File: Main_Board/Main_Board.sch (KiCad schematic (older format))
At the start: 40 parts, among them J3 BATT_IN, Q1 Q_PMOS_GDS, U1 TEENSY_4_1_MASTER, U2 TEENSY_4_1_SLAVE

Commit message: Started Light PCB
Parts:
- added R?: 100k, symbol Device:R_Small
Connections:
- wire segments 215 -> 223
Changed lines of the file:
@@
 	11600 2400 11600 2300
 Wire Wire Line
-	11600 3200 11600 3100
+	11600 3200 11600 3150
 $Comp
 L Switch:SW_SPST SW?
@@
 Text GLabel 2500 6850 0    50   Input ~ 0
 P4
-Text GLabel 2000 5250 0    50   Input ~ 0
+Text GLabel 2500 6450 0    50   Input ~ 0
 ~WR
-Text GLabel 1850 5350 0    50   Input ~ 0
+Text GLabel 4700 6650 2    50   Input ~ 0
 ~CS
-Text GLabel 1850 5150 0    50   Input ~ 0
+Text GLabel 2350 6350 0    50   Input ~ 0
 ~EN
 Text GLabel 4300 8050 2    50   Input ~ 0
 D
-Text GLabel 2000 4950 0    50   Input ~ 0
+Text GLabel 4300 6550 2    50   Input ~ 0
 LIGHT_EN
 Text GLabel 5350 6750 0    50   Output ~ 0
@@
 	1    0    0    -1
 $EndComp
+Wire Wire Line
+	4300 6550 4200 6550
+Wire Wire Line
+	2500 6450 2600 6450
+Wire Wire Line
+	2350 6350 2600 6350
+Wire Wire Line
+	4700 6650 4200 6650
+$Comp
+L power:+VDC #PWR?
+U 1 1 6200D369
+P 11250 3100
+F 0 "#PWR?" H 11250 3000 50  0001 C CNN
+F 1 "+VDC" H 11250 3375 50  0000 C CNN
+F 2 "" H 11250 3100 50  0001 C CNN
+F 3 "" H 11250 3100 50  0001 C CNN
+	1    11250 3100
+	1    0    0    -1
+$EndComp
+$Comp
+L Device:R_Small R?
+U 1 1 6200E122
+P 11400 3150
+F 0 "R?" H 11459 3196 50  0000 L CNN
+F 1 "100k" H 11459 3105 50  0000 L CNN
+F 2 "" H 11400 3150 50  0001 C CNN
+F 3 "~" H 11400 3150 50  0001 C CNN
+	1    11400 3150
+	0    1    1    0
+$EndComp
+Wire Wire Line
+	11500 3150 11600 3150
+Connection ~ 11600 3150
+Wire Wire Line
+	11600 3150 11600 3100
+Wire Wire Line
+	11250 3100 11250 3150
+Wire Wire Line
+	11250 3150 11300 3150
 $EndSCHEMATC

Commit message: Finalizing Main PCB Sch
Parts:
- added J?: HR-SR04_R_CONN, symbol Connector_Generic:Conn_01x04
- added J?: HR-SR04_L_CONN, symbol Connector_Generic:Conn_01x04
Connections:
- net labels added: ECHO_L, ECHO_R, TRIG_L, TRIG_R
- wire segments 223 -> 239
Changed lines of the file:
@@
 	1    0    0    -1
 $EndComp
+Text GLabel 12950 8550 0    50   Output ~ 0
+P0
 Text GLabel 12950 8450 0    50   Output ~ 0
-P0
-Text GLabel 12950 8550 0    50   Output ~ 0
 P1
+Text GLabel 12950 8750 0    50   Output ~ 0
+P2
 Text GLabel 12950 8650 0    50   Output ~ 0
-P2
-Text GLabel 12950 8750 0    50   Output ~ 0
 P3
 Text GLabel 12950 8850 0    50   Output ~ 0
@@
 Text GLabel 4300 8050 2    50   Input ~ 0
 D
-Text GLabel 4300 6550 2    50   Input ~ 0
-LIGHT_EN
 Text GLabel 5350 6750 0    50   Output ~ 0
 HOLD_SW
@@
 Wire Wire Line
 	8500 7500 8550 7500
-Text GLabel 8450 6300 0    50   Input ~ 0
+Text GLabel 8450 6300 0    50   Output ~ 0
 MAGN_SDA
-Text GLabel 8450 6400 0    50   Input ~ 0
+Text GLabel 8450 6400 0    50   Output ~ 0
 MAGN_SCL
 Wire Wire Line
@@
 Wire Wire Line
 	8450 6400 8550 6400
-$Comp
-L power:+5V #PWR?
-U 1 1 62126097
-P 8500 6150
-F 0 "#PWR?" H 8500 6000 50  0001 C CNN
-F 1 "+5V" H 8515 6323 50  0000 C CNN
-F 2 "" H 8500 6150 50  0001 C CNN
-F 3 "" H 8500 6150 50  0001 C CNN
-	1    8500 6150
-	1    0    0    -1
-$EndComp
 Wire Wire Line
 	8500 6150 8500 6200
@@
 Wire Wire Line
 	8500 6500 8550 6500
-Text GLabel 7200 8150 2    50   Input ~ 0
+Text GLabel 7200 8150 2    50   Output ~ 0
 OLED_SDA
-Text GLabel 7200 8250 2    50   Input ~ 0
+Text GLabel 7200 8250 2    50   Output ~ 0
 OLED_SCL
 Text GLabel 7200 8050 2    50   Input ~ 0
@@
 Wire Wire Line
 	11250 3150 11300 3150
+$Comp
+L Connector_Generic:Conn_01x04 J?
+U 1 1 62000862
+P 9950 6300
+F 0 "J?" H 10030 6292 50  0000 L CNN
+F 1 "HR-SR04_R_CONN" H 10030 6201 50  0000 L CNN
+F 2 "" H 9950 6300 50  0001 C CNN
+F 3 "~" H 9950 6300 50  0001 C CNN
+	1    9950 6300
+	1    0    0    -1
+$EndComp
+$Comp
+L Connector_Generic:Conn_01x04 J?
+U 1 1 62000F7B
+P 9950 7350
+F 0 "J?" H 10030 7342 50  0000 L CNN
+F 1 "HR-SR04_L_CONN" H 10030 7251 50  0000 L CNN
+F 2 "" H 9950 7350 50  0001 C CNN
+F 3 "~" H 9950 7350 50  0001 C CNN
+	1    9950 7350
+	1    0    0    -1
+$EndComp
+$Comp
+L power:+3.3V #PWR?
+U 1 1 62001B8E
+P 8500 6150
+F 0 "#PWR?" H 8500 6000 50  0001 C CNN
+F 1 "+3.3V" H 8515 6323 50  0000 C CNN
+F 2 "" H 8500 6150 50  0001 C CNN
+F 3 "" H 8500 6150 50  0001 C CNN
+	1    8500 6150
+	1    0    0    -1
+$EndComp
+$Comp
+L power:GND #PWR?
+U 1 1 62002A38
+P 9700 6550
+F 0 "#PWR?" H 9700 6300 50  0001 C CNN
+F 1 "GND" H 9705 6377 50  0000 C CNN
+F 2 "" H 9700 6550 50  0001 C CNN
+F 3 "" H 9700 6550 50  0001 C CNN
+	1    9700 6550
+	1    0    0    -1
+$EndComp
+$Comp
+L power:+5V #PWR?
+U 1 1 62002DEB
+P 9700 7200
+F 0 "#PWR?" H 9700 7050 50  0001 C CNN
+F 1 "+5V" H 9715 7373 50  0000 C CNN
+F 2 "" H 9700 7200 50  0001 C CNN
+F 3 "" H 9700 7200 50  0001 C CNN
+	1    9700 7200
+	1    0    0    -1
+$EndComp
+$Comp
+L power:GND #PWR?
+U 1 1 6200332C
+P 9700 7600
+F 0 "#PWR?" H 9700 7350 50  0001 C CNN
+F 1 "GND" H 9705 7427 50  0000 C CNN
+F 2 "" H 9700 7600 50  0001 C CNN
+F 3 "" H 9700 7600 50  0001 C CNN
+	1    9700 7600
+	1    0    0    -1
+$EndComp
+$Comp
+L power:+5V #PWR?
+U 1 1 62003657
+P 9700 6150
+F 0 "#PWR?" H 9700 6000 50  0001 C CNN
+F 1 "+5V" H 9715 6323 50  0000 C CNN
+F 2 "" H 9700 6150 50  0001 C CNN
+F 3 "" H 9700 6150 50  0001 C CNN
+	1    9700 6150
+	1    0    0    -1
+$EndComp
+Wire Wire Line
+	9700 6150 9700 6200
+Wire Wire Line
+	9700 6200 9750 6200
+Wire Wire Line
+	9700 6550 9700 6500
+Wire Wire Line
+	9700 6500 9750 6500
+Wire Wire Line
+	9700 7200 9700 7250
+Wire Wire Line
+	9700 7250 9750 7250
+Wire Wire Line
+	9700 7600 9700 7550
+Wire Wire Line
+	9700 7550 9750 7550
+Text GLabel 9650 7350 0    50   Output ~ 0
+TRIG_L
+Text GLabel 9650 6300 0    50   Output ~ 0
+TRIG_R
+Text GLabel 9650 6400 0    50   Output ~ 0
+ECHO_R
+Text GLabel 9650 7450 0    50   Output ~ 0
+ECHO_L
+Wire Wire Line
+	9650 6300 9750 6300
+Wire Wire Line
+	9650 6400 9750 6400
+Wire Wire Line
+	9650 7350 9750 7350
+Wire Wire Line
+	9650 7450 9750 7450
+Text GLabel 2500 7350 0    50   Input ~ 0
+ECHO_R
+Text GLabel 2500 7250 0    50   Input ~ 0
+TRIG_R
+Wire Wire Line
+	2500 7250 2600 7250
+Wire Wire Line
+	2500 7350 2600 7350
+Text GLabel 2500 6650 0    50   Input ~ 0
+ECHO_L
+Text GLabel 4300 6550 2    50   Input ~ 0
+LIGHT_EN
+Text GLabel 2500 6550 0    50   Input ~ 0
+TRIG_L
+Wire Wire Line
+	2500 6550 2600 6550
+Wire Wire Line
+	2500 6650 2600 6650
 $EndSCHEMATC

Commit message: Finalized Pin layout, started redesigned Buck
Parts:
- removed C?: 0.1u, symbol Device:C
- removed C?: 47u, symbol Device:C
- removed C?: 10n, symbol Device:C_Small
- removed C?: 6.8n, symbol Device:C_Small
- removed C?: 22u, symbol Device:C
- removed L?: 8.2u, symbol Device:L
- removed R?: 100k, symbol Device:R
- removed R?: 45.3k, symbol Device:R_Small
- removed R?: 10k, symbol Device:R_Small
- removed R?: 6.8k, symbol Device:R_Small
- removed U?: AP6503, symbol Regulator_Switching:AP6503
- added C? (x8): C_Small, symbol Device:C_Small
- added D? (x2): WS2812B, LED_SMD:LED_WS2812B_PLCC4_5.0x5.0mm_P3.2mm, symbol LED:WS2812B
- added L?: L_Small, symbol Device:L_Small
- added R? (x5): R_Small, symbol Device:R_Small
- added U?: SiC467ED, symbol Main_Board:SiC467ED
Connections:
- wire segments 239 -> 284
- no-connect marks 19 -> 20
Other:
- moved on the sheet: D1, D?, J3, J?, Q1, Q?, R1, R?, SW?, U?

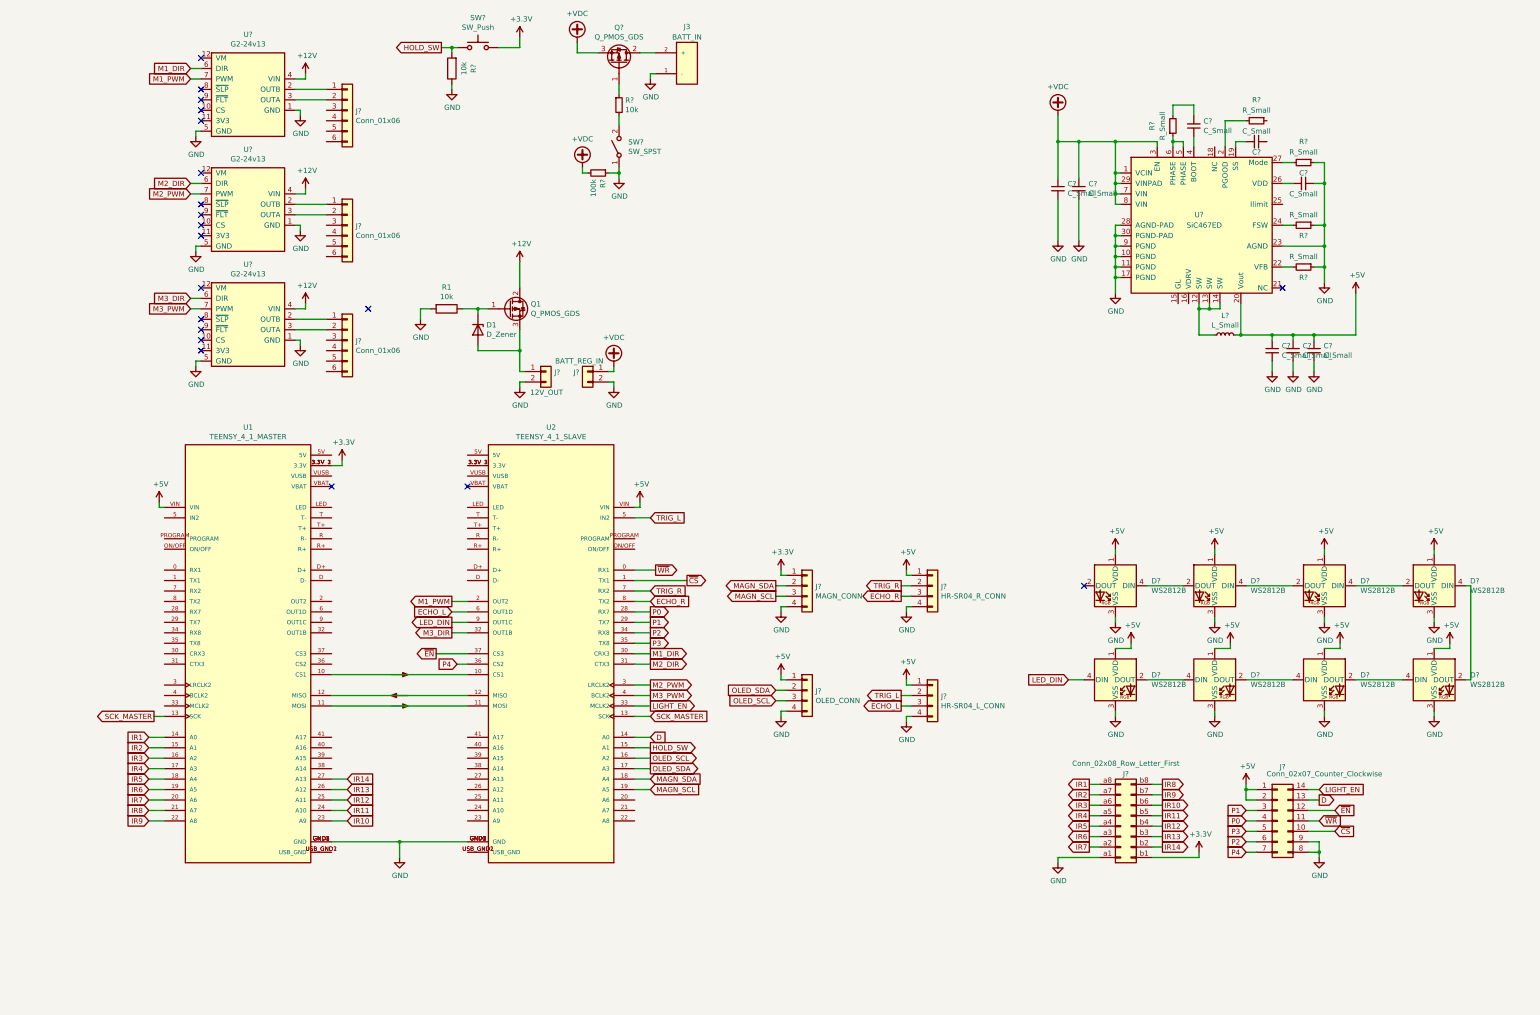
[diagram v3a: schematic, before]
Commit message: added light gate
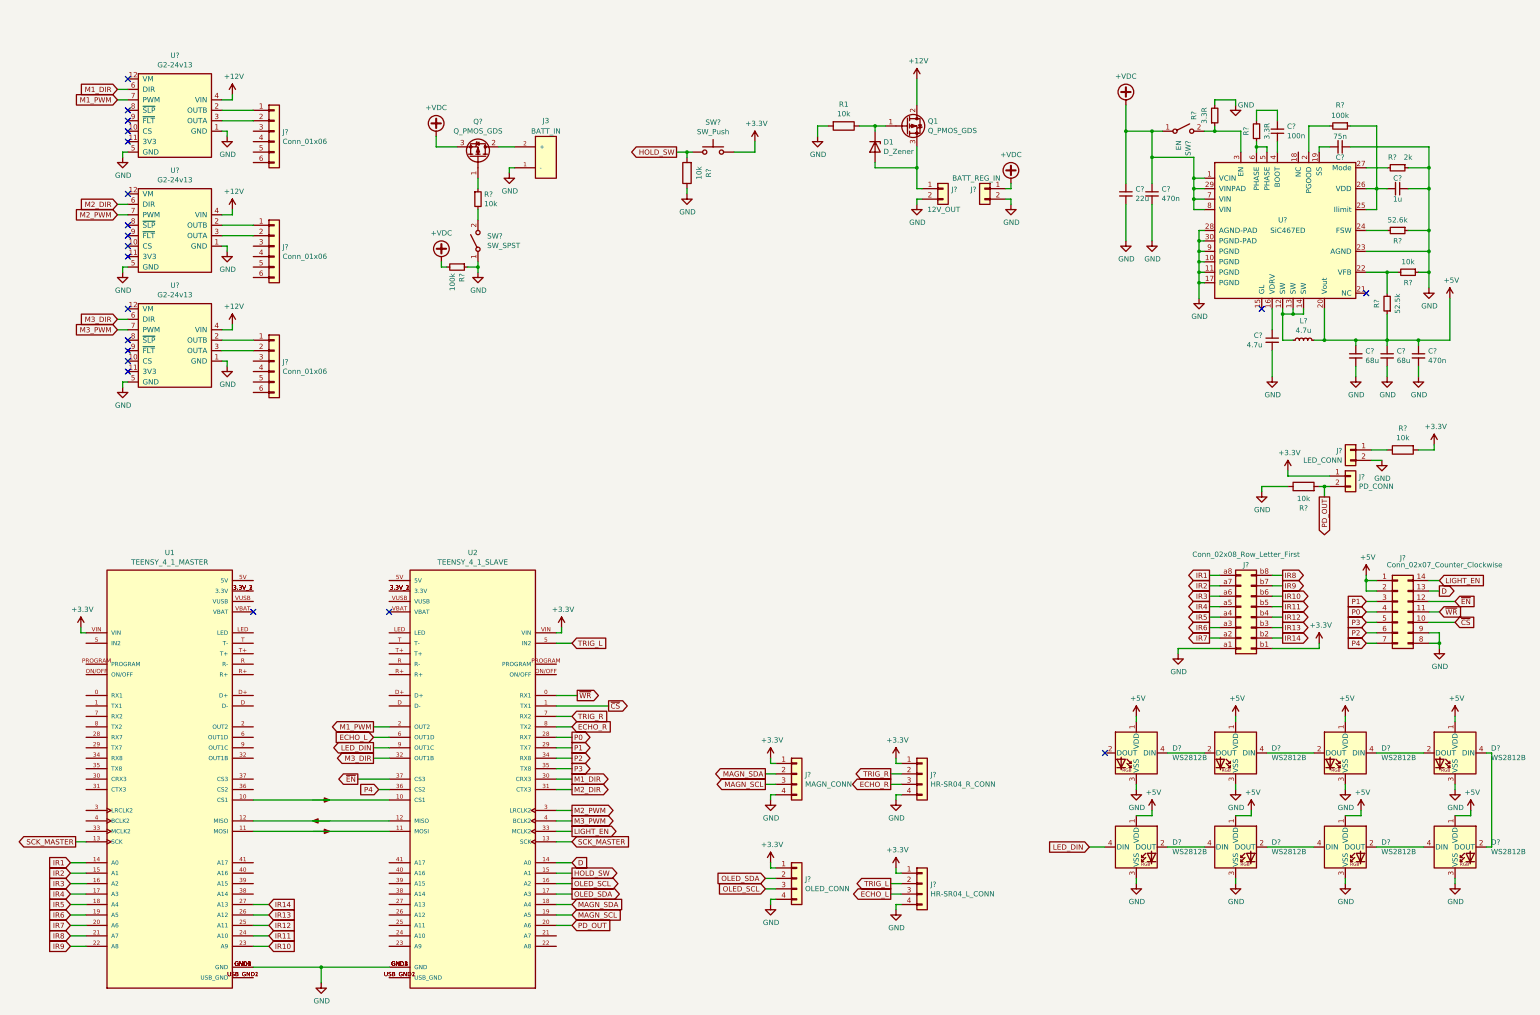
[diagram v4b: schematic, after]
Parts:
- added C?: 4.7u, symbol Device:C_Small
- added J?: PD_CONN, symbol Connector_Generic:Conn_01x02
- added J?: LED_CONN, symbol Connector_Generic:Conn_01x02
- added R?: 52.5k, symbol Device:R_Small
- added R?: 3.3R, symbol Device:R_Small
- added R? (x2): 10k, symbol Device:R
- added SW?: EN, symbol Switch:SW_SPST
- C?: value C_Small -> 22u
- C? (x2): value C_Small -> 470n
- C? (x2): value C_Small -> 68u
- C?: value C_Small -> 1u
- C?: value C_Small -> 75n
- C?: value C_Small -> 100n
- L?: value L_Small -> 4.7u
- R?: value R_Small -> 52.6k
- R?: value R_Small -> 2k
- R?: value R_Small -> 10k
- R?: value R_Small -> 3.3R
- R?: value R_Small -> 100k
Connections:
- net +3V3: now also J?.1 (Pin_1), J?.1 (Pin_1), J?.1 (Pin_1), U1.VIN, U2.VIN, J?.1 (Pin_1), R?.2; no longer U1.3.3V_1 (3.3V), U1.3.3V_2 (3.3V), U1.3.3V_3 (3.3V)
- net +5V: now also R?.1; no longer J?.1 (Pin_1), J?.1 (Pin_1), J?.1 (Pin_1), U1.VIN, U2.VIN
- net +VDC: now also SW?.1 (A); no longer U?.3 (EN)
- net GND: now also C?.1, C?.2, J?.2 (Pin_2), R?.1, R?.2
- net PD_OUT: now reaches U2.20 (A6)
- net PD_OUT: now also J?.2 (Pin_2), R?.2
- net at U?.16 (VDRV): now also C?.1
- net at R?.2, U?.22 (VFB): now also R?.2
- net at U?.25 (Ilimit): now also C?.2, R?.1, U?.26 (VDD)
- new net: U1.3.3V_1 (3.3V), U1.3.3V_2 (3.3V), U1.3.3V_3 (3.3V)
- new net: R?.1, SW?.2 (B), U?.3 (EN)
- new net: J?.1 (Pin_1), R?.1
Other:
- moved on the sheet: C?, D1, D?, J3, J?, L?, Q1, Q?, R1, R?, SW?, U1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

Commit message: Finished Main PCB schematic
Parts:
- C?: value 22u -> 10u
- C? (x2): value 68u -> 22u
- C?: value 470n -> 220n
- L?: value 4.7u -> 2.2u
- R?: value 52.5k -> 17k5
- R?: value 3.3R -> 100k
- R?: value 52.6k -> 34k7
- R?: value 10k -> 5k6
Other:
- note added: "12V Buck-Boost"
- note added: "3.3V Buck"
- note added: "Battery Input"
- note added: "Compass"
- note added: "Connectors"
- note added: "Hold Switch"
- note added: "Indicator LEDs"
- note added: "Light Gate Connectors"
- note added: "Microcontrollers"
- note added: "Motor Drivers"
- note added: "OLED"
- note added: "PCB Connectors"
- note added: "Sonar Left"
- note added: "Sonar Right"
- moved on the sheet: D?, J?, U1, U2

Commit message: Some small alterations to the main pcb sch
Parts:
- removed D1: D_Zener, symbol Device:D_Zener
- removed R1: 10k, symbol Device:R
- added D1, D10, D11: LED, LED_SMD:LED_0805_2012Metric, symbol Device:LED
- added D12: 20V, symbol Device:D_Zener_Small
- added R1, R15, R16, R17: 10k, symbol Device:R_Small
- added R14, R18: 100k, symbol Device:R_Small
- added SW4: SW_SPST, symbol Switch:SW_SPST
- C1, C6, C7: renamed from C?; footprint (none) -> Capacitor_SMD:C_1210_3225Metric
- C2, C3, C4, C5, C8, C9: renamed from C?; footprint (none) -> Capacitor_SMD:C_0603_1608Metric
- J1, J2, J3: renamed from J?; footprint (none) -> Connector_JST:JST_EH_S6B-EH_1x06_P2.50mm_Horizontal
- J10, J9: renamed from J?; footprint (none) -> Connector_PinSocket_2.54mm:PinSocket_1x04_P2.54mm_Vertical
- J13, J14: renamed from J?; footprint (none) -> Connector_JST:JST_EH_S2B-EH_1x02_P2.50mm_Horizontal
- J4: renamed from J3; footprint (none) -> Main_Board:AMASS_XT60-M
- J5: renamed from J?; footprint (none) -> Connector_Hirose:Hirose_DF11-16DP-2DSA_2x08_P2.00mm_Vertical
- J6, J7: renamed from J?; footprint (none) -> Connector_JST:JST_EH_B4B-EH-A_1x04_P2.50mm_Vertical
- J8: renamed from J?; footprint (none) -> Connector_Hirose:Hirose_DF11-14DP-2DSA_2x07_P2.00mm_Vertical
- L1: renamed from L?; footprint (none) -> Main_Board:Bours_SRP4020FA
- gave numbers to parts that had none: 30
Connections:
- net +5V is gone; now on net +3V3: C6.1, C7.1, C9.1, D2.1 (VDD), D3.1 (VDD), D4.1 (VDD), D5.1 (VDD), D6.1 (VDD), D7.1 (VDD), D8.1 (VDD), D9.1 (VDD), J8.1 (Pin_1), J8.2 (Pin_2), L1.2, R9.1, U6.20 (Vout)
- net +12V: now also Q1.3 (S), R15.1; no longer Q1.2 (D)
- net +3V3: now also R17.1
- net +VDC: now also D12.2 (A), R16.1, R18.1
- net GND: now also D1.1 (K), D10.1 (K), D11.1 (K), SW4.1 (A); no longer R2.1
- net at Q1.1 (G): now also R1.1, R14.1
- net at J11.1 (Pin_1): now also Q1.2 (D), R14.2; no longer Q1.3 (S)
- net at Q2.1 (G), R3.1: now also D12.1 (K)
- net at R3.2, SW1.2 (B): now also R2.1, R18.2
- net M1_A: now reaches J1.1 (Pin_1)
- net M1_A: now also U3.3 (OUTA); no longer U3.2 (OUTB)
- net M1_B: now reaches J1.2 (Pin_2)
- net M1_B: now also U3.2 (OUTB); no longer U3.3 (OUTA)
- net M2_A: now reaches J2.1 (Pin_1)
- net M2_A: now also U4.3 (OUTA); no longer U4.2 (OUTB)
- net M2_B: now reaches J2.2 (Pin_2)
- net M2_B: now also U4.2 (OUTB); no longer U4.3 (OUTA)
- net M3_A: now reaches J3.1 (Pin_1)
- net M3_A: now also U5.3 (OUTA); no longer U5.2 (OUTB)
- net M3_B: now reaches J3.2 (Pin_2)
- net M3_B: now also U5.2 (OUTB); no longer U5.3 (OUTA)
- new net: R1.2, SW4.2 (B)
- new net: D1.2 (A), R15.2
- new net: D10.2 (A), R16.2
- new net: D11.2 (A), R17.2
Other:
- note added: "Motor 1"
- note added: "Motor 2"
- note added: "Motor 3"
- moved on the sheet: J1, J11, J12, J2, J3, J4, J5, J8, Q2, R2, R3, R4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
